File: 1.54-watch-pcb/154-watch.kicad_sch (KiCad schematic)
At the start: 67 parts, among them J1 AFC24-S24FIC-00, J2 Conn_01x06_Female, J3 USB_C_Programming, J4 Jack-DC, J5 Conn_01x02_Male, Q1 Si1308, Q2 BC817, Q3 BC817, Q4 Si2301CDS, SW1 RESET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

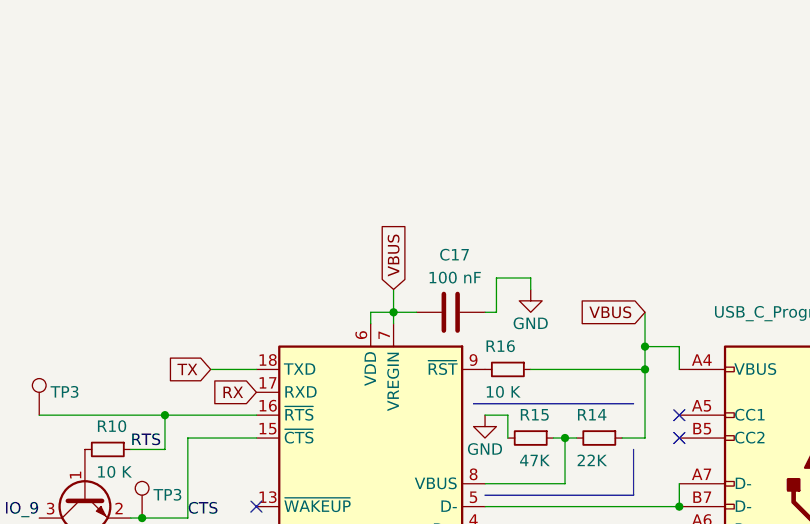
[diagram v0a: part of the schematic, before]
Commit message: VregIN is the only power input CP2102
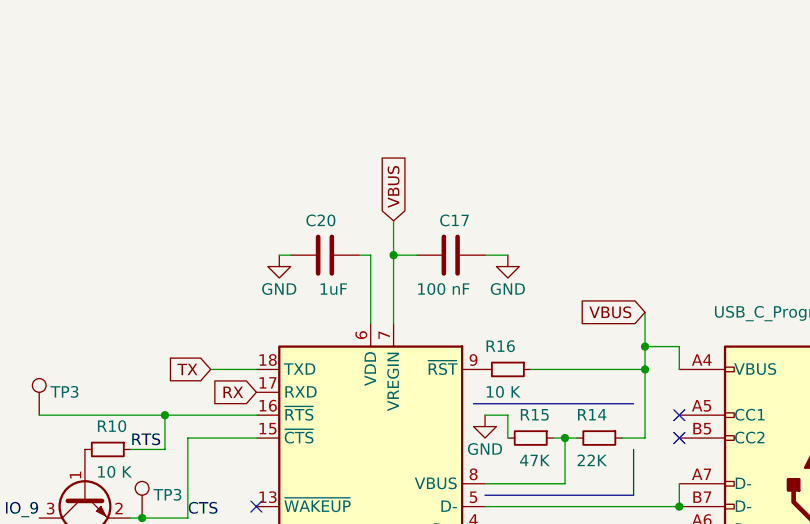
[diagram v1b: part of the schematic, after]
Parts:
- added C20: 1uF, Capacitor_SMD:C_0402_1005Metric, symbol Device:C
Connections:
- net GND: now also C20.2
- net VBUS: no longer U3.6 (VDD)
- new net: C20.1, U3.6 (VDD)
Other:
- moved on the sheet: C17
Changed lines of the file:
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@@
   (junction (at 105.41 184.15) (diameter 0) (color 0 0 0 0)
   )
+  (junction (at 344.17 52.07) (diameter 0) (color 0 0 0 0)
+  )
   (junction (at 231.14 71.12) (diameter 0) (color 0 0 0 0)
   )
@@
   (junction (at 49.53 186.69) (diameter 0) (color 0 0 0 0)
   )
-  (junction (at 344.17 58.42) (diameter 0) (color 0 0 0 0)
-  )
   (junction (at 170.18 184.15) (diameter 0) (color 0 0 0 0)
   )
@@
     (stroke (width 0) (type default))
   )
-  (wire (pts (xy 355.6 58.42) (xy 355.6 54.61))
-    (stroke (width 0) (type default))
-  )
   (wire (pts (xy 241.3 100.33) (xy 228.6 100.33))
     (stroke (width 0) (type default))
@@
     (stroke (width 0) (type default))
   )
-  (wire (pts (xy 344.17 55.88) (xy 344.17 58.42))
+  (wire (pts (xy 344.17 48.26) (xy 344.17 52.07))
     (stroke (width 0) (type default))
   )
@@
     (stroke (width 0) (type default))
   )
-  (wire (pts (xy 341.63 59.69) (xy 341.63 58.42))
+  (wire (pts (xy 341.63 52.07) (xy 341.63 59.69))
     (stroke (width 0) (type default))
   )
@@
     (stroke (width 0) (type default))
   )
-  (wire (pts (xy 344.17 58.42) (xy 344.17 59.69))
-    (stroke (width 0) (type default))
-  )
   (wire (pts (xy 281.94 67.31) (xy 281.94 62.23))
     (stroke (width 0) (type default))
@@
     (stroke (width 0) (type default))
   )
+  (wire (pts (xy 340.36 52.07) (xy 341.63 52.07))
+    (stroke (width 0) (type default))
+  )
   (wire (pts (xy 69.85 111.76) (xy 69.85 110.49))
     (stroke (width 0) (type default))
@@
     (stroke (width 0) (type default))
   )
+  (wire (pts (xy 331.47 52.07) (xy 332.74 52.07))
+    (stroke (width 0) (type default))
+  )
   (wire (pts (xy 172.72 59.69) (xy 182.88 59.69))
     (stroke (width 0) (type default))
@@
     (stroke (width 0) (type default))
   )
-  (wire (pts (xy 355.6 54.61) (xy 359.41 54.61))
-    (stroke (width 0) (type default))
-  )
   (polyline (pts (xy 92.71 208.28) (xy 92.71 228.6))
     (stroke (width 0) (type default))
@@
     (stroke (width 0) (type default))
   )
-  (wire (pts (xy 354.33 58.42) (xy 355.6 58.42))
+  (wire (pts (xy 354.33 52.07) (xy 356.87 52.07))
     (stroke (width 0) (type default))
   )
@@
     (stroke (width 0) (type default))
   )
+  (wire (pts (xy 344.17 52.07) (xy 344.17 59.69))
+    (stroke (width 0) (type default))
+  )
   (wire (pts (xy 147.32 104.14) (xy 144.78 104.14))
     (stroke (width 0) (type default))
@@
     (stroke (width 0) (type default))
   )
-  (wire (pts (xy 344.17 58.42) (xy 346.71 58.42))
+  (wire (pts (xy 344.17 52.07) (xy 346.71 52.07))
     (stroke (width 0) (type default))
   )
@@
     (stroke (width 0) (type default))
   )
-  (wire (pts (xy 359.41 54.61) (xy 359.41 55.88))
-    (stroke (width 0) (type default))
-  )
   (wire (pts (xy 281.94 128.27) (xy 281.94 125.73))
     (stroke (width 0) (type default))
@@
     (stroke (width 0) (type default))
   )
-  (wire (pts (xy 341.63 58.42) (xy 344.17 58.42))
-    (stroke (width 0) (type default))
-  )
   (wire (pts (xy 281.94 90.17) (xy 281.94 87.63))
     (stroke (width 0) (type default))
@@
     )
   )
-  (global_label "VBUS" (shape input) (at 344.17 55.88 90) (fields_autoplaced)
+  (global_label "VBUS" (shape input) (at 344.17 48.26 90) (fields_autoplaced)
     (effects (font (size 1.27 1.27)) (justify left))
-    (property "Intersheetrefs" "${INTERSHEET_REFS}" (at 344.2494 48.5683 90)
+    (property "Intersheetrefs" "${INTERSHEET_REFS}" (at 344.2494 40.9483 90)
       (effects (font (size 1.27 1.27)) (justify left) hide)
     )
@@
     )
   )
-  (symbol (lib_id "power:GND") (at 359.41 55.88 0) (unit 1)
+  (symbol (lib_id "power:GND") (at 356.87 52.07 0) (unit 1)
     (in_bom yes) (on_board yes) (dnp no)
-    (property "Reference" "#PWR030" (at 359.41 62.23 0)
+    (property "Reference" "#PWR030" (at 356.87 58.42 0)
       (effects (font (size 1.27 1.27)) hide)
     )
-    (property "Value" "GND" (at 359.41 59.69 0)
+    (property "Value" "GND" (at 356.87 55.88 0)
       (effects (font (size 1.27 1.27)))
     )
-    (property "Footprint" "" (at 359.41 55.88 0)
+    (property "Footprint" "" (at 356.87 52.07 0)
       (effects (font (size 1.27 1.27)) hide)
     )
-    (property "Datasheet" "" (at 359.41 55.88 0)
+    (property "Datasheet" "" (at 356.87 52.07 0)
       (effects (font (size 1.27 1.27)) hide)
     )
@@
     )
   )
-  (symbol (lib_id "Device:C") (at 350.52 58.42 90) (unit 1)
+  (symbol (lib_id "Device:C") (at 350.52 52.07 90) (unit 1)
     (in_bom yes) (on_board yes) (dnp no)
-    (property "Reference" "C17" (at 349.25 52.07 90)
+    (property "Reference" "C17" (at 349.25 48.26 90)
       (effects (font (size 1.27 1.27)) (justify right))
     )
-    (property "Value" "100 nF" (at 347.98 54.61 90)
+    (property "Value" "100 nF" (at 346.71 55.88 90)
       (effects (font (size 1.27 1.27)) (justify right))
     )
-    (property "Footprint" "Capacitor_SMD:C_0805_2012Metric" (at 354.33 57.4548 0)
+    (property "Footprint" "Capacitor_SMD:C_0805_2012Metric" (at 354.33 51.1048 0)
       (effects (font (size 1.27 1.27)) hide)
     )
-    (property "Datasheet" "~" (at 350.52 58.42 0)
+    (property "Datasheet" "~" (at 350.52 52.07 0)
       (effects (font (size 1.27 1.27)) hide)
     )
-    (property "LCSC" "C28233" (at 350.52 58.42 0)
+    (property "LCSC" "C28233" (at 350.52 52.07 0)
       (effects (font (size 1.27 1.27)) hide)
     )
@@
     )
   )
+  (symbol (lib_id "Device:C") (at 336.55 52.07 270) (unit 1)
+    (in_bom yes) (on_board yes) (dnp no)
+    (property "Reference" "C20" (at 337.82 48.26 90)
+      (effects (font (size 1.27 1.27)) (justify right))
+    )
+    (property "Value" "1uF" (at 339.09 55.88 90)
+      (effects (font (size 1.27 1.27)) (justify right))
+    )
+    (property "Footprint" "Capacitor_SMD:C_0402_1005Metric" (at 332.74 53.0352 0)
+      (effects (font (size 1.27 1.27)) hide)
+    )
+    (property "Datasheet" "~" (at 336.55 52.07 0)
+      (effects (font (size 1.27 1.27)) hide)
+    )
+    (property "LCSC" "C527012" (at 336.55 52.07 0)
+      (effects (font (size 1.27 1.27)) hide)
+    )
+    (pin "1")
+    (pin "2")
+    (instances
+      (project "154-watch"
+        (path "/ea6fde00-59dc-4a79-a647-7e38199fae0e"
+          (reference "C20") (unit 1)
+        )
+      )
+    )
+  )
   (symbol (lib_id "Device:C") (at 73.66 110.49 270) (unit 1)
     (in_bom yes) (on_board yes) (dnp no)
@@
         )
       )
+    )
+  )
+  (symbol (lib_id "power:GND") (at 331.47 52.07 0) (unit 1)
+    (in_bom yes) (on_board yes) (dnp no)
+    (property "Reference" "#PWR037" (at 331.47 58.42 0)
+      (effects (font (size 1.27 1.27)) hide)
+    )
+    (property "Value" "GND" (at 331.47 55.88 0)
+      (effects (font (size 1.27 1.27)))
+    )
+    (property "Footprint" "" (at 331.47 52.07 0)
+      (effects (font (size 1.27 1.27)) hide)
+    )
+    (property "Datasheet" "" (at 331.47 52.07 0)
+      (effects (font (size 1.27 1.27)) hide)
+    )
+    (pin "1")
+    (instances
+      (project "154-watch"
+        (path "/ea6fde00-59dc-4a79-a647-7e38199fae0e"
+          (reference "#PWR037") (unit 1)
+        )
+      )

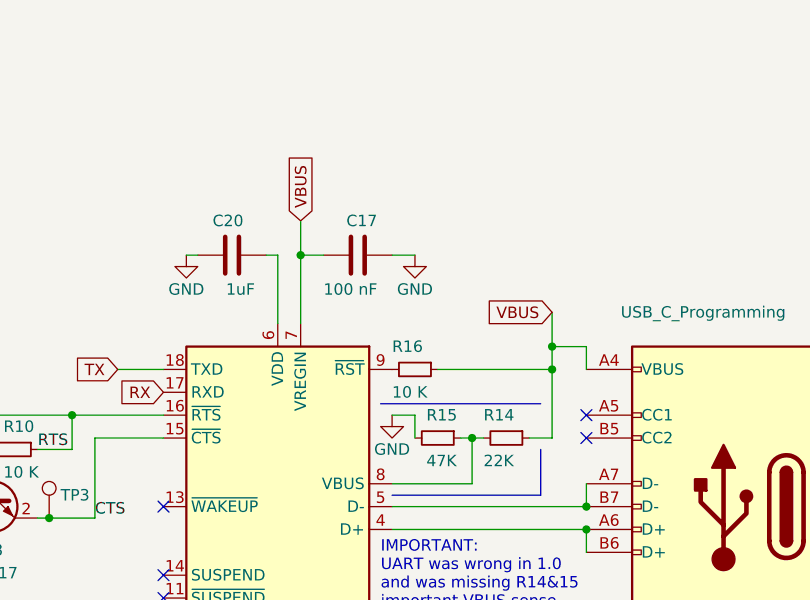
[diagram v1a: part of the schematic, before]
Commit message: RST is pulled-up now to logic level 3V3
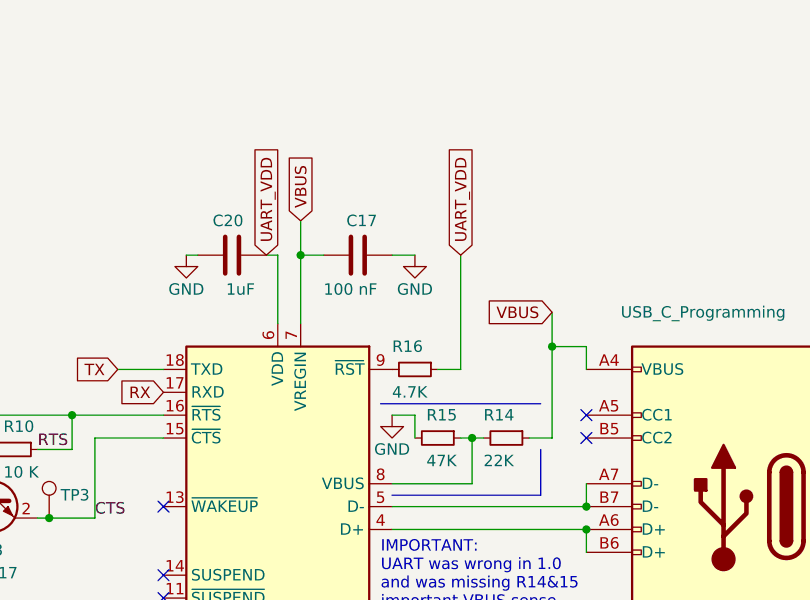
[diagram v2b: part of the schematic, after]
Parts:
- R16: value 10 K -> 4.7K; LCSC C319933 -> C149892
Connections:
- net VBUS: no longer R16.1
- net UART_VDD: now reaches C20.1, U3.6 (VDD)
- net UART_VDD: now also R16.1
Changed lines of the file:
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@@
   (junction (at 287.02 143.51) (diameter 0) (color 0 0 0 0)
   )
-  (junction (at 372.11 64.77) (diameter 0) (color 0 0 0 0)
-  )
   (junction (at 281.94 128.27) (diameter 0) (color 0 0 0 0)
   )
@@
     (stroke (width 0) (type default))
   )
-  (wire (pts (xy 372.11 72.39) (xy 372.11 64.77))
+  (wire (pts (xy 372.11 62.23) (xy 372.11 72.39))
     (stroke (width 0) (type default))
   )
@@
     (stroke (width 0) (type default))
   )
+  (wire (pts (xy 359.41 64.77) (xy 361.95 64.77))
+    (stroke (width 0) (type default))
+  )
   (wire (pts (xy 58.42 116.84) (xy 58.42 118.11))
     (stroke (width 0) (type default))
@@
     (stroke (width 0) (type default))
   )
-  (wire (pts (xy 372.11 64.77) (xy 372.11 62.23))
-    (stroke (width 0) (type default))
-  )
   (wire (pts (xy 67.31 167.64) (xy 83.82 167.64))
     (stroke (width 0) (type default))
@@
     (stroke (width 0) (type default))
   )
+  (wire (pts (xy 361.95 64.77) (xy 361.95 52.07))
+    (stroke (width 0) (type default))
+  )
   (wire (pts (xy 58.42 68.58) (xy 62.23 68.58))
     (stroke (width 0) (type default))
@@
     (stroke (width 0) (type default))
   )
-  (wire (pts (xy 359.41 64.77) (xy 372.11 64.77))
-    (stroke (width 0) (type default))
-  )
   (wire (pts (xy 92.71 167.64) (xy 92.71 163.83))
     (stroke (width 0) (type default))
@@
     )
   )
+  (global_label "UART_VDD" (shape input) (at 340.36 52.07 90) (fields_autoplaced)
+    (effects (font (size 1.27 1.27)) (justify left))
+    (property "Intersheetrefs" "${INTERSHEET_REFS}" (at 340.36 39.9113 90)
+      (effects (font (size 1.27 1.27)) (justify left) hide)
+    )
+  )
   (global_label "VBAT" (shape input) (at 71.12 224.79 0) (fields_autoplaced)
     (effects (font (size 1.27 1.27)) (justify left))
@@
     )
   )
+  (global_label "UART_VDD" (shape input) (at 361.95 52.07 90) (fields_autoplaced)
+    (effects (font (size 1.27 1.27)) (justify left))
+    (property "Intersheetrefs" "${INTERSHEET_REFS}" (at 361.95 39.9113 90)
+      (effects (font (size 1.27 1.27)) (justify left) hide)
+    )
+  )
   (global_label "VBUS" (shape input) (at 151.13 179.07 180) (fields_autoplaced)
     (effects (font (size 1.27 1.27)) (justify right))
@@
       (effects (font (size 1.27 1.27)) (justify left))
     )
-    (property "Value" "10 K" (at 354.33 67.31 90)
+    (property "Value" "4.7K" (at 354.33 67.31 90)
       (effects (font (size 1.27 1.27)) (justify left))
     )
@@
       (effects (font (size 1.27 1.27)) hide)
     )
-    (property "Datasheet" "https://jlcpcb.com/partdetail/VikingTech-AR02DTD1002/C319933" (at 356.87 64.77 0)
+    (property "Datasheet" "https://jlcpcb.com/partdetail/Ever_OhmsTech-ST0402J4K70Q10Z/C149892" (at 356.87 64.77 0)
       (effects (font (size 1.27 1.27)) hide)
     )
-    (property "LCSC" "C319933" (at 356.87 64.77 90)
+    (property "LCSC" "C149892" (at 356.87 64.77 90)
       (effects (font (size 1.27 1.27)) hide)
     )
